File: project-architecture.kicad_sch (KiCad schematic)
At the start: 0 parts

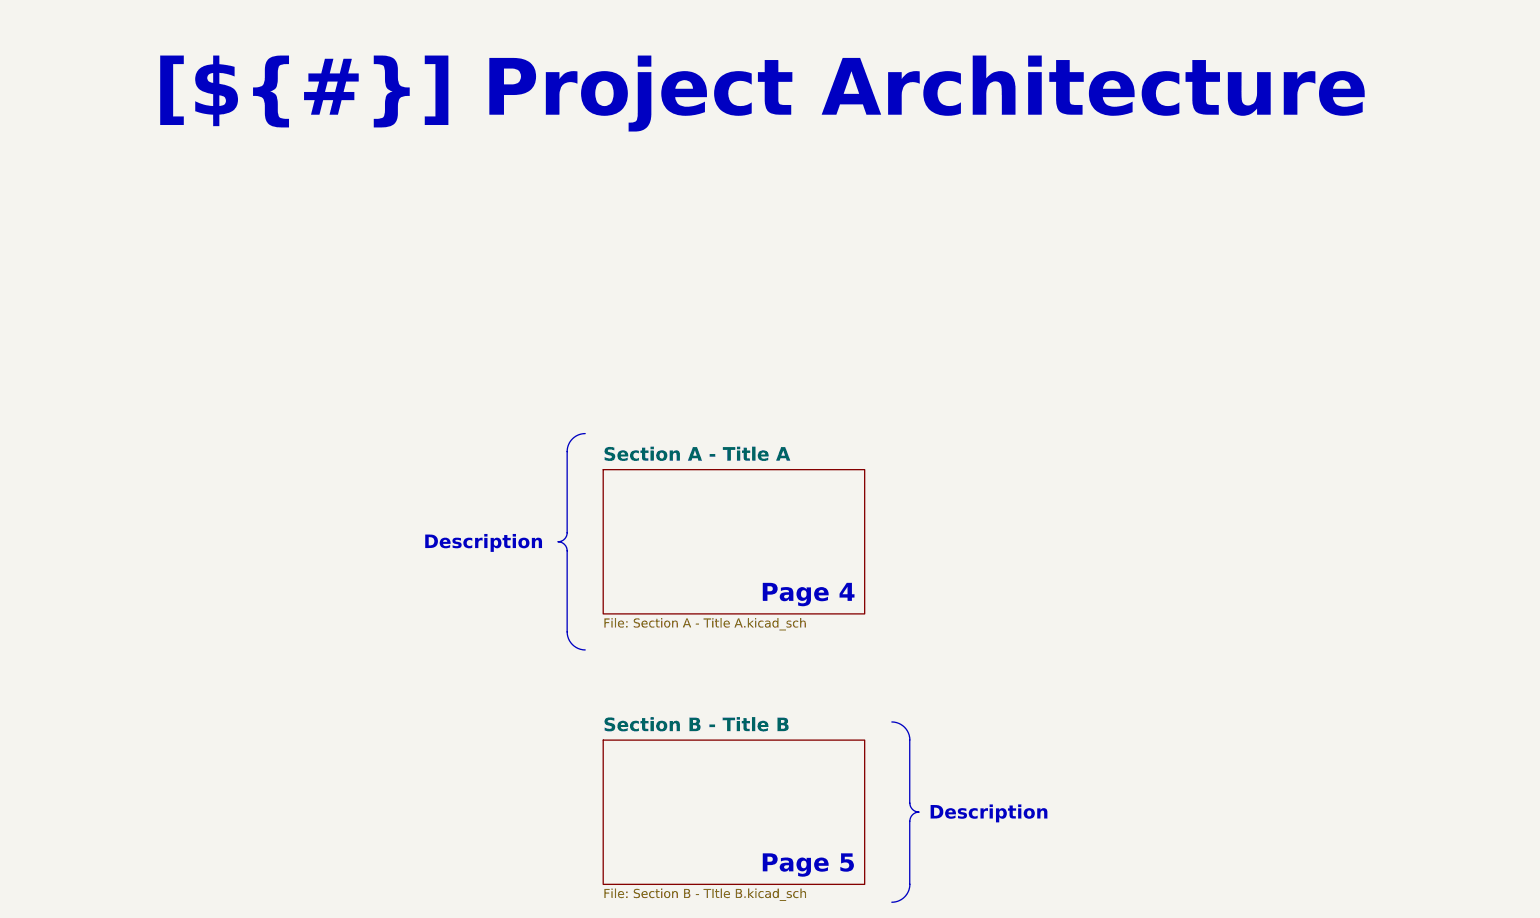
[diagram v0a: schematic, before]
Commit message: feat: convert template to Boardwright
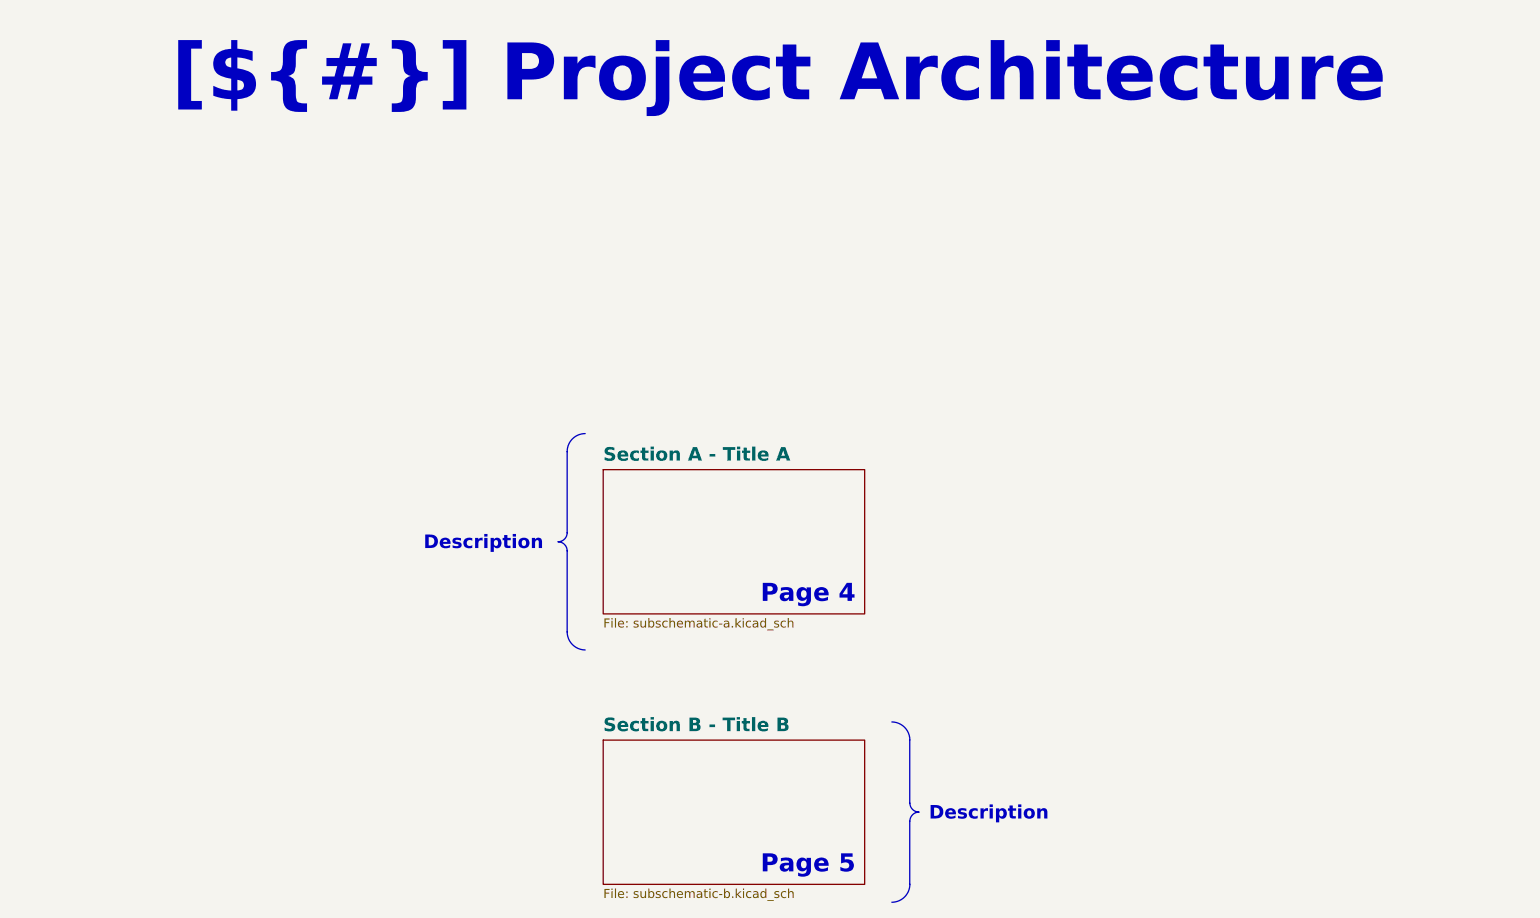
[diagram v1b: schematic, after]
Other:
- sheet Section A - Title A: file Section A - Title A.kicad_sch -> subschematic-a.kicad_sch
- sheet Section B - Title B: file Section B - TItle B.kicad_sch -> subschematic-b.kicad_sch
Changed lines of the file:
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@@
 	(text_box "[${#}] ${TITLE}"
 		(exclude_from_sim no)
-		(at 121.92 15 0)
-		(size 181.61 15)
+		(at 20.32 10.16 0)
+		(size 389.89 20.32)
 		(margins 5.9999 5.9999 5.9999 5.9999)
 		(stroke
@@
 			)
 		)
-		(property "Sheetfile" "Section B - TItle B.kicad_sch"
+		(property "Sheetfile" "subschematic-b.kicad_sch"
 			(at 190.5 135.2046 0)
 			(effects
@@
 		)
 		(instances
-			(project "KDT_Hierarchical_KiBot"
+			(project "boardwright"
 				(path "/f9e05184-c88b-4a88-ae9c-ab2bdb32be7c/c5103ceb-5325-4a84-a025-9638a412984e"
 					(page "5")
@@
 			)
 		)
-		(property "Sheetfile" "Section A - Title A.kicad_sch"
+		(property "Sheetfile" "subschematic-a.kicad_sch"
 			(at 190.5 97.1046 0)
 			(effects
@@
 		)
 		(instances
-			(project "KDT_Hierarchical_KiBot"
+			(project "boardwright"
 				(path "/f9e05184-c88b-4a88-ae9c-ab2bdb32be7c/c5103ceb-5325-4a84-a025-9638a412984e"
 					(page "4")
